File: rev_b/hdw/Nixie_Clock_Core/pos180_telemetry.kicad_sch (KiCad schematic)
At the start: 4 parts, among them U502 MCP9804, U701 MCP3427-xUN

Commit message: lots of rev B control board schematic progress
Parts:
- added C? (x3): 0.1uF, Capacitors_SMD:C_0402, symbol Custom_Library:C_Custom
- added DOC?: 0x69, symbol Custom_Library:I2C_Address
- added R? (x2): 1k, Resistors_SMD:R_0402, symbol Custom_Library:R_Custom
- added R?: 75k, Resistors_SMD:R_0402, symbol Custom_Library:R_Custom
- added R?: 150k, Resistors_SMD:R_0402, symbol Custom_Library:R_Custom
- U?: renamed from U701; Configuration (none) -> Telemetry
- renumbered C503 to C?, DOC502 to DOC?, U502 to U?
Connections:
- net +3.3V: now also U?.6 (VDD), C?.1
- net GND: now also U?.2 (CH1-), U?.3 (VSS), U?.5 (CH2-), U?.9 (Adr0), C?.2, C?.2, C?.2, R?.2, R?.2
- net I2C_SCL: now also U?.8 (SCL)
- net I2C_SDA: now also U?.7 (SDA)
- net at U?.1 (CH1+): now also C?.1, R?.1, R?.2
- net at U?.4 (CH2+): now also C?.1, R?.1, R?.2
- new net +180V: R?.1, R?.1
- no-connect marks 1 -> 2
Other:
- moved on the sheet: U?

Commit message: more carrier board progress
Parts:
- removed R?: 1k, Resistors_SMD:R_0402, symbol Custom_Library:R_Custom
- added R?: 1k, Resistors_SMD:R_0402, symbol Custom_Library:R_Custom
- R? (x3): Configuration (none) -> Telemetry
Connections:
- net GND: now also R?.2
- net at C?.1, R?.2, U?.1 (CH1+): now also R?.1
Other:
- note removed: "USE THIS TO MONITOR +180V AND +90V"
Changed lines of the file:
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@@
     (stroke (width 0) (type default))
-  )
-  (text "USE THIS TO MONITOR +180V AND +90V" (at 82.55 31.75 0)
-    (effects (font (face "Courier New") (size 5.08 5.08) (thickness 0.254) bold (color 255 37 56 1)) (justify left bottom))
   )
   (global_label "I2C_SDA" (shape bidirectional) (at 151.13 62.23 0)
@@
     (property "Digi-Key PN" "RMCF0402FT1K00CT-ND" (at 71.12 60.96 0)
       (effects (font (size 1.524 1.524)) hide)
+    )
+    (property "Configuration" "Telemetry" (at 76.2 71.12 90)
+      (effects (font (size 1.27 1.27)))
     )
     (pin "1")
@@
     )
   )
-  (symbol (lib_id "Custom_Library:R_Custom") (at 66.04 71.12 0) (mirror y) (unit 1)
-    (in_bom yes) (on_board yes) (dnp no)
-    (property "Reference" "R?" (at 67.564 71.12 0)
-      (effects (font (size 1.27 1.27)) (justify right))
-    )
-    (property "Value" "1k" (at 66.04 71.12 90)
-      (effects (font (size 1.27 1.27)))
-    )
-    (property "Footprint" "Resistors_SMD:R_0402" (at 66.04 71.12 0)
-      (effects (font (size 1.27 1.27)) hide)
-    )
-    (property "Datasheet" "" (at 66.04 71.12 0)
-      (effects (font (size 1.27 1.27)) hide)
-    )
-    (property "display_footprint" "0402" (at 64.262 69.088 0)
-      (effects (font (size 1.27 1.27)) (justify left) hide)
-    )
-    (property "Tolerance" "1%" (at 64.262 71.12 0)
-      (effects (font (size 1.27 1.27)) (justify left) hide)
-    )
-    (property "Wattage" "1/16W" (at 64.262 72.898 0)
-      (effects (font (size 1.27 1.27)) (justify left) hide)
-    )
-    (property "Digi-Key PN" "RMCF0402FT1K00CT-ND" (at 58.42 60.96 0)
-      (effects (font (size 1.524 1.524)) hide)
-    )
-    (pin "1")
-    (pin "2")
-    (instances
-      (project "Nixie_Clock_Core"
-        (path "/16fdce21-b570-4d81-a458-e8839d611806/2cd2cc24-63f3-4ff7-b2ec-a0dfd71a27e5"
-          (reference "R?") (unit 1)
-        )
-        (path "/16fdce21-b570-4d81-a458-e8839d611806/4cb440c2-4356-400c-9387-edaaa635d5a5"
-          (reference "R?") (unit 1)
-        )
-        (path "/16fdce21-b570-4d81-a458-e8839d611806/2f89509e-1daf-4eca-8cda-923804eff633"
-          (reference "R?") (unit 1)
-        )
-      )
-      (project "LED_Panel_Controller"
-        (path "/22e05ee1-b227-4be7-9418-94433f274720/00000000-0000-0000-0000-00005baae1dc"
-          (reference "R?") (unit 1)
-        )
-        (path "/22e05ee1-b227-4be7-9418-94433f274720/00000000-0000-0000-0000-00005bb844fd"
-          (reference "R?") (unit 1)
-        )
-        (path "/22e05ee1-b227-4be7-9418-94433f274720/00000000-0000-0000-0000-00005cad2d97"
-          (reference "R?") (unit 1)
-        )
-        (path "/22e05ee1-b227-4be7-9418-94433f274720/00000000-0000-0000-0000-00005cb7a8c3"
-          (reference "R?") (unit 1)
-        )
-        (path "/22e05ee1-b227-4be7-9418-94433f274720/00000000-0000-0000-0000-00005f582e4a"
-          (reference "R?") (unit 1)
-        )
-        (path "/22e05ee1-b227-4be7-9418-94433f274720/00000000-0000-0000-0000-00005baae16c"
-          (reference "R?") (unit 1)
-        )
-        (path "/22e05ee1-b227-4be7-9418-94433f274720/00000000-0000-0000-0000-00005cb7a8bc"
-          (reference "R?") (unit 1)
-        )
-        (path "/22e05ee1-b227-4be7-9418-94433f274720/00000000-0000-0000-0000-00005baae1f3"
-          (reference "R?") (unit 1)
-        )
-        (path "/22e05ee1-b227-4be7-9418-94433f274720/00000000-0000-0000-0000-00005e93cc4e"
-          (reference "R?") (unit 1)
-        )
-        (path "/22e05ee1-b227-4be7-9418-94433f274720/00000000-0000-0000-0000-00005bf346b3"
-          (reference "R?") (unit 1)
-        )
-      )
-    )
-  )
   (symbol (lib_id "power:+3.3V") (at 140.97 146.05 0) (unit 1)
     (in_bom yes) (on_board yes) (dnp no)
@@
     (property "Digi-Key PN" "" (at 71.12 43.815 0)
       (effects (font (size 1.524 1.524)) hide)
+    )
+    (property "Configuration" "Telemetry" (at 76.2 54.61 90)
+      (effects (font (size 1.27 1.27)))
     )
     (pin "1")
@@
     )
   )
+  (symbol (lib_id "Custom_Library:R_Custom") (at 66.04 71.12 0) (mirror y) (unit 1)
+    (in_bom yes) (on_board yes) (dnp no)
+    (property "Reference" "R?" (at 67.564 71.12 0)
+      (effects (font (size 1.27 1.27)) (justify right))
+    )
+    (property "Value" "1k" (at 66.04 71.12 90)
+      (effects (font (size 1.27 1.27)))
+    )
+    (property "Footprint" "Resistors_SMD:R_0402" (at 66.04 71.12 0)
+      (effects (font (size 1.27 1.27)) hide)
+    )
+    (property "Datasheet" "" (at 66.04 71.12 0)
+      (effects (font (size 1.27 1.27)) hide)
+    )
+    (property "display_footprint" "0402" (at 64.262 69.088 0)
+      (effects (font (size 1.27 1.27)) (justify left) hide)
+    )
+    (property "Tolerance" "1%" (at 64.262 71.12 0)
+      (effects (font (size 1.27 1.27)) (justify left) hide)
+    )
+    (property "Wattage" "1/16W" (at 64.262 72.898 0)
+      (effects (font (size 1.27 1.27)) (justify left) hide)
+    )
+    (property "Digi-Key PN" "RMCF0402FT1K00CT-ND" (at 58.42 60.96 0)
+      (effects (font (size 1.524 1.524)) hide)
+    )
+    (property "Configuration" "Telemetry" (at 63.5 71.12 90)
+      (effects (font (size 1.27 1.27)))
+    )
+    (pin "1")
+    (pin "2")
+    (instances
+      (project "Nixie_Clock_Core"
+        (path "/16fdce21-b570-4d81-a458-e8839d611806/2cd2cc24-63f3-4ff7-b2ec-a0dfd71a27e5"
+          (reference "R?") (unit 1)
+        )
+        (path "/16fdce21-b570-4d81-a458-e8839d611806/4cb440c2-4356-400c-9387-edaaa635d5a5"
+          (reference "R?") (unit 1)
+        )
+        (path "/16fdce21-b570-4d81-a458-e8839d611806/2f89509e-1daf-4eca-8cda-923804eff633"
+          (reference "R?") (unit 1)
+        )
+      )
+      (project "LED_Panel_Controller"
+        (path "/22e05ee1-b227-4be7-9418-94433f274720/00000000-0000-0000-0000-00005baae1dc"
+          (reference "R?") (unit 1)
+        )
+        (path "/22e05ee1-b227-4be7-9418-94433f274720/00000000-0000-0000-0000-00005bb844fd"
+          (reference "R?") (unit 1)
+        )
+        (path "/22e05ee1-b227-4be7-9418-94433f274720/00000000-0000-0000-0000-00005cad2d97"
+          (reference "R?") (unit 1)
+        )
+        (path "/22e05ee1-b227-4be7-9418-94433f274720/00000000-0000-0000-0000-00005cb7a8c3"
+          (reference "R?") (unit 1)
+        )
+        (path "/22e05ee1-b227-4be7-9418-94433f274720/00000000-0000-0000-0000-00005f582e4a"
+          (reference "R?") (unit 1)
+        )
+        (path "/22e05ee1-b227-4be7-9418-94433f274720/00000000-0000-0000-0000-00005baae16c"
+          (reference "R?") (unit 1)
+        )
+        (path "/22e05ee1-b227-4be7-9418-94433f274720/00000000-0000-0000-0000-00005cb7a8bc"
+          (reference "R?") (unit 1)
+        )
+        (path "/22e05ee1-b227-4be7-9418-94433f274720/00000000-0000-0000-0000-00005baae1f3"
+          (reference "R?") (unit 1)
+        )
+        (path "/22e05ee1-b227-4be7-9418-94433f274720/00000000-0000-0000-0000-00005e93cc4e"
+          (reference "R?") (unit 1)
+        )
+        (path "/22e05ee1-b227-4be7-9418-94433f274720/00000000-0000-0000-0000-00005bf346b3"
+          (reference "R?") (unit 1)
+        )
+      )
+    )
+  )
   (symbol (lib_id "power:GND") (at 78.74 74.93 0) (mirror y) (unit 1)
     (in_bom yes) (on_board yes) (dnp no)
@@
       (effects (font (size 1.524 1.524)) hide)
     )
-    (pin "1")
+    (property "Configuration" "Telemetry" (at 63.5 54.61 90)
+      (effects (font (size 1.27 1.27)))
+    )
+    (pin "1")

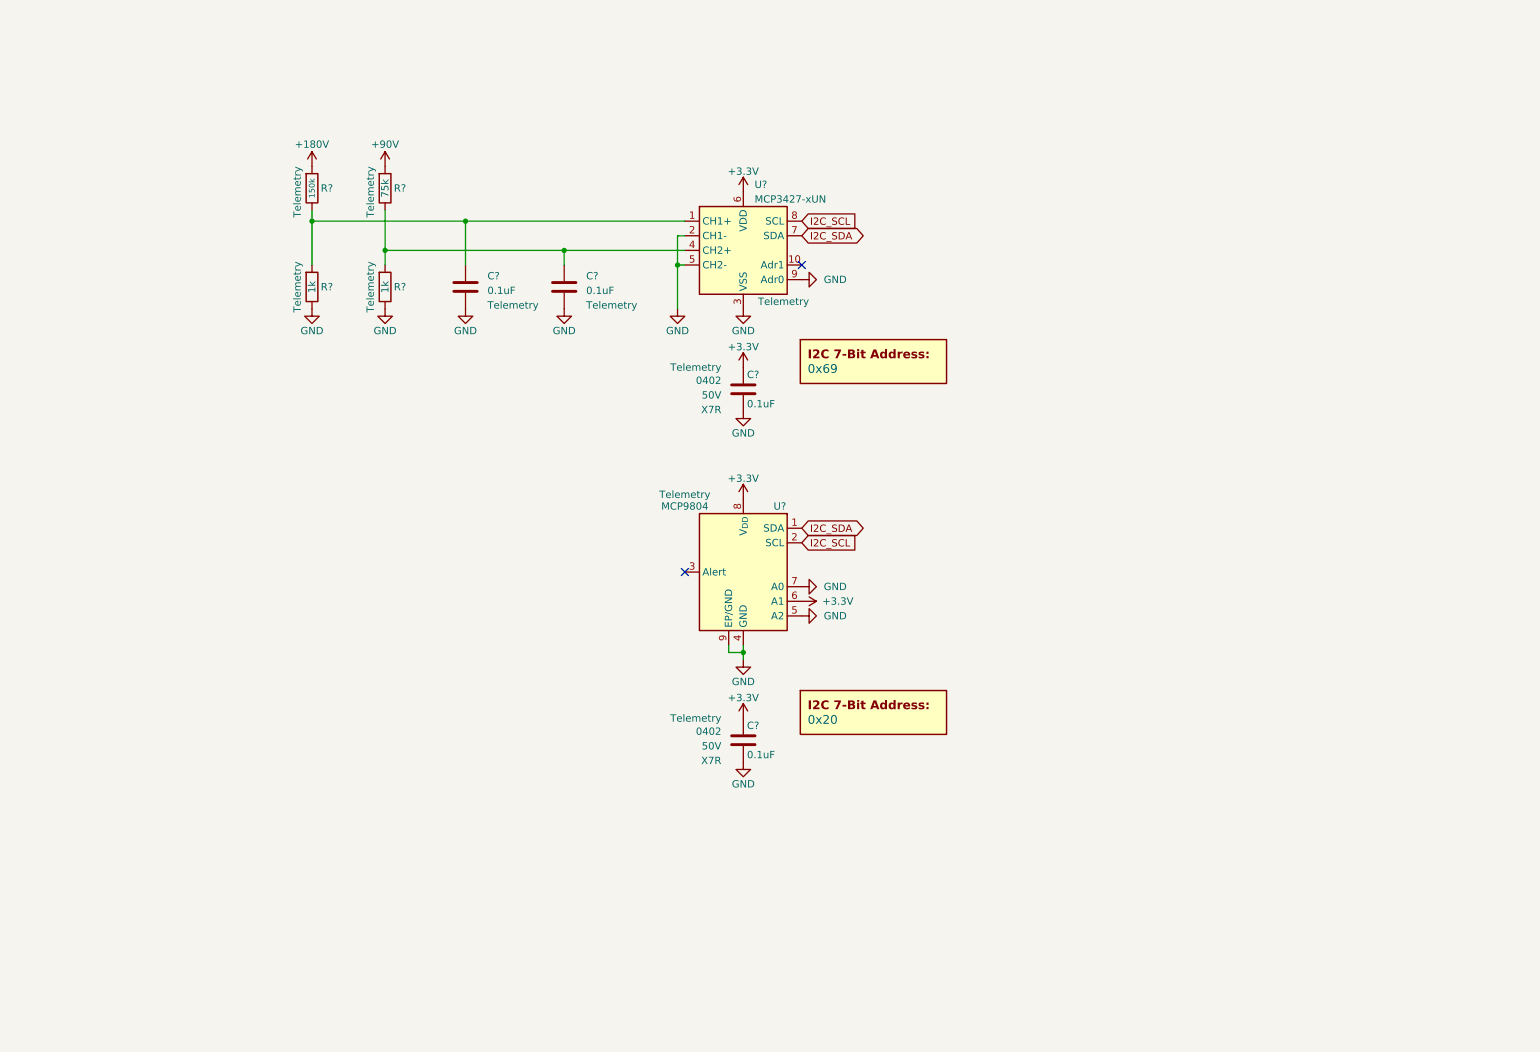
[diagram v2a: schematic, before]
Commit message: revamped POS180 telemetry
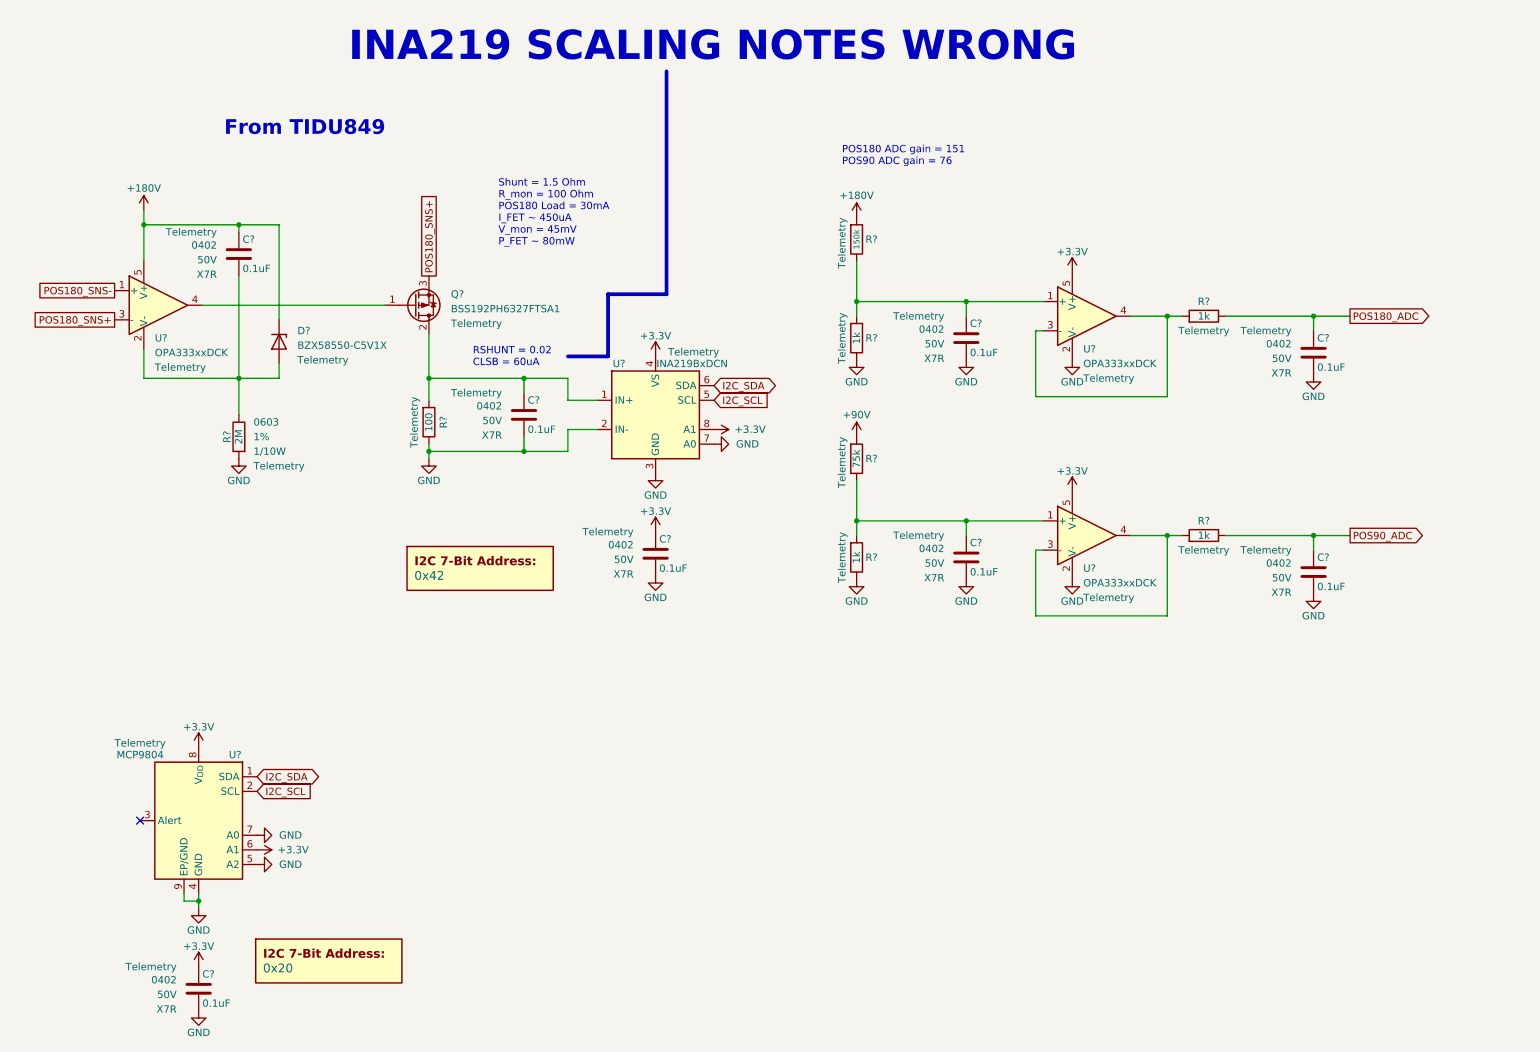
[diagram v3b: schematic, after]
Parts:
- removed C? (x3): 0.1uF, Capacitors_SMD:C_0402, symbol Custom_Library:C_Custom
- removed DOC?: 0x69, symbol Custom_Library:I2C_Address
- removed R? (x2): 1k, Resistors_SMD:R_0402, symbol Custom_Library:R_Custom
- removed R?: 75k, Resistors_SMD:R_0402, symbol Custom_Library:R_Custom
- removed R?: 150k, Resistors_SMD:R_0402, symbol Custom_Library:R_Custom
- removed U?: MCP3427-xUN, Package_SO:MSOP-10_3x3mm_P0.5mm, symbol Analog_ADC:MCP3427-xUN
- added C? (x7): 0.1uF, Capacitors_SMD:C_0402, symbol Custom_Library:C_Custom
- added D?: BZX58550-C5V1X, Diodes_SMD:D_SOD-523, symbol Device:D_Zener
- added DOC?: 0x42, symbol Custom_Library:I2C_Address
- added Q?: BSS192PH6327FTSA1, Package_TO_SOT_SMD:SOT-89-3, symbol Device:Q_PMOS_GDS
- added R?: 150k, Resistors_SMD:R_0402, symbol Custom_Library:R_Custom
- added R? (x4): 1k, Resistors_SMD:R_0402, symbol Custom_Library:R_Custom
- added R?: 75k, Resistors_SMD:R_0402, symbol Custom_Library:R_Custom
- added R?: 100, Resistors_SMD:R_0402, symbol Custom_Library:R_Custom
- added R?: 2M, Resistors_SMD:R_0603, symbol Nixie-Clock-rescue:R
- added U? (x3): OPA333xxDCK, Package_TO_SOT_SMD:SOT-353_SC-70-5, symbol Amplifier_Operational:OPA333xxDCK
- added U?: INA219BxDCN, Package_TO_SOT_SMD:SOT-23-8, symbol Analog_ADC:INA219BxDCN
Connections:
- net +180V: now also C?.1, D?.1 (K), R?.1, R?.1, U?.5 (V+)
- net +3.3V: now also C?.1, U?.4 (VS), U?.5 (V+), U?.5 (V+), U?.8 (A1)
- net GND: now also C?.2, C?.2, C?.2, C?.2, C?.2, C?.2, R?.2, R?.2, R?.2, R?.2, U?.2 (IN-), U?.2 (V-), U?.2 (V-), U?.3 (GND), U?.7 (A0)
- net I2C_SCL: now also U?.5 (SCL)
- net I2C_SDA: now also U?.6 (SDA)
- new net: Q?.1 (G), U?.4
- new net: C?.1, Q?.2 (D), R?.1, U?.1 (IN+)
- new net: C?.1, R?.1, R?.2, U?.1 (+) (x2)
- new net: R?.1, U?.3 (-), U?.4 (x2)
- new net: C?.2, D?.2 (A), R?.1, U?.2 (V-)
- new net: C?.1, R?.2
- new net POS180_SNS+: Q?.3 (S), U?.3 (-)
- new net POS180_SNS-: U?.1 (+)
- new net POS90_ADC: C?.1, R?.2
- no-connect marks 2 -> 1
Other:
- note added: "From TIDU849"
- note added: "INA219 SCALING NOTES WRONG"
- note added: "POS180 ADC gain = 151 POS90 ADC gain = 76"
- note added: "RSHUNT = 0.02 CLSB = 60uA"
- note added: "Shunt = 1.5 Ohm R_mon = 100 Ohm POS180 Load = 30mA I_FET ~ 450uA V_mon = 45mV P_FET ~ 80mW"
- moved on the sheet: C?, U?

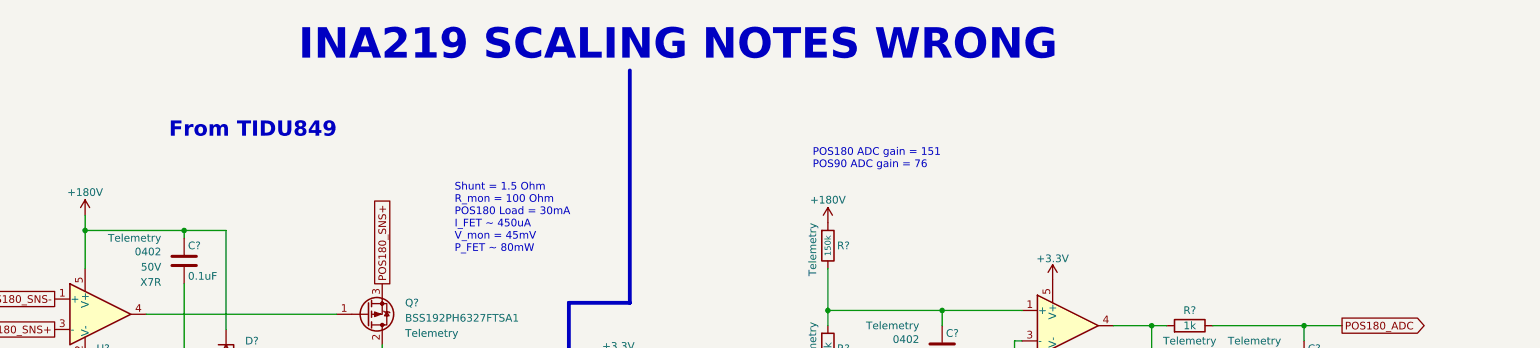
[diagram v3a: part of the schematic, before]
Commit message: more schematic progress, assigning signals to MCU"
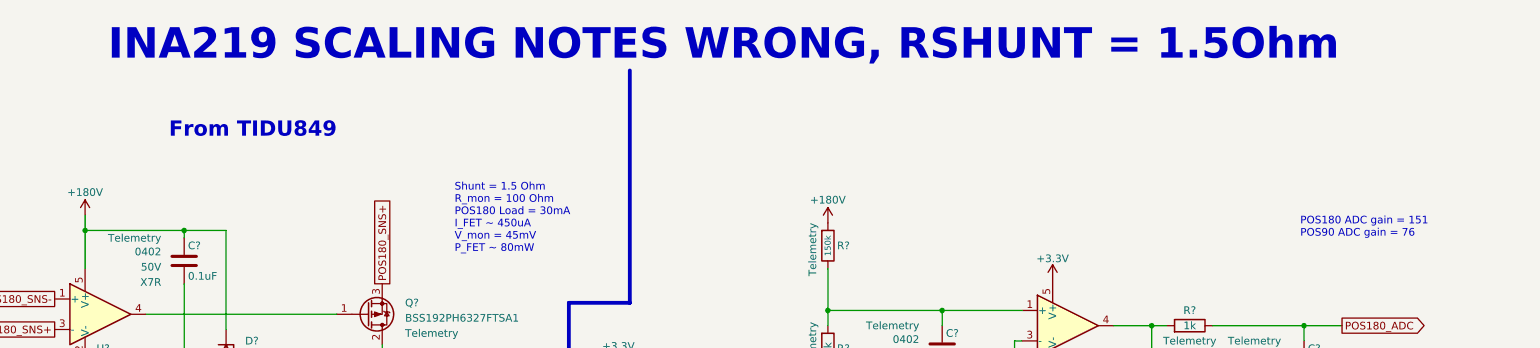
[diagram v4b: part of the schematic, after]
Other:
- note added: "INA219 SCALING NOTES WRONG, RSHUNT = 1.5Ohm"
- note removed: "INA219 SCALING NOTES WRONG"
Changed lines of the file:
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@@
     (stroke (width 0) (type default))
   )
-  (text "POS180 ADC gain = 151\nPOS90 ADC gain = 76" (at 158.115 50.165 0)
+  (text "POS180 ADC gain = 151\nPOS90 ADC gain = 76" (at 239.395 61.595 0)
     (effects (font (size 1.27 1.27)) (justify left bottom))
   )
@@
     (effects (font (size 1.27 1.27)) (justify left bottom))
   )
-  (text "INA219 SCALING NOTES WRONG" (at 72.39 32.385 0)
+  (text "INA219 SCALING NOTES WRONG, RSHUNT = 1.5Ohm" (at 40.64 32.385 0)
     (effects (font (face "Courier New") (size 5.08 5.08) (thickness 0.254) bold (color 255 37 56 1)) (justify left bottom))
   )
